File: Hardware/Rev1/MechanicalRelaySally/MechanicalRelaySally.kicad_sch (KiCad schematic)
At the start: 0 parts

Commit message: A
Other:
- added sheet Microcontroller (microcontroller.kicad_sch)
- sheet Power Routing ports: added CONTROL_BUS; removed none
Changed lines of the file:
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@@
 	(generator_version "9.0")
 	(paper "A4")
+	(bus
+		(pts
+			(xy 81.28 53.34) (xy 101.6 53.34)
+		)
+		(stroke
+			(width 0)
+			(type default)
+		)
+	)
 	(sheet
-		(at 132.08 25.4)
+		(at 53.34 50.8)
 		(size 27.94 22.86)
 		(exclude_from_sim no)
@@
 		)
 		(property "Sheetname" "Power Routing"
-			(at 132.08 24.6884 0)
+			(at 53.34 50.0884 0)
 			(effects
 				(font
@@
 		)
 		(property "Sheetfile" "power_routing.kicad_sch"
-			(at 132.08 48.8446 0)
+			(at 53.34 74.2446 0)
 			(effects
 				(font
@@
 				)
 				(justify left top)
+			)
+		)
+		(pin "CONTROL_BUS" input
+			(at 81.28 53.34 0)
+			(effects
+				(font
+					(size 1.27 1.27)
+				)
+				(justify right)
 			)
 		)
@@
 				)
 			)
+		)
+	)
+	(sheet
+		(at 101.6 50.8)
+		(size 27.94 22.86)
+		(exclude_from_sim no)
+		(in_bom yes)
+		(on_board yes)
+		(dnp no)
+		(fields_autoplaced yes)
+		(stroke
+			(width 0.1524)
+			(type solid)
+		)
+		(fill
+			(color 255 255 194 1.0000)
+		)
+		(property "Sheetname" "Microcontroller"
+			(at 101.6 50.0884 0)
+			(effects
+				(font
+					(size 1.27 1.27)
+				)
+				(justify left bottom)
+			)
+		)
+		(property "Sheetfile" "microcontroller.kicad_sch"
+			(at 101.6 74.2446 0)
+			(effects
+				(font
+					(size 1.27 1.27)
+				)
+				(justify left top)
+			)
+		)
+		(pin "CONTROL_BUS" input
+			(at 101.6 53.34 180)
+			(effects
+				(font
+					(size 1.27 1.27)
+				)
+				(justify left)
+			)
+		)
+		(instances
+			(project "MechanicalRelaySally"
+				(path "/fc3bfb83-1db4-4bd1-b480-85f699496fec"
+					(page "8")
+				)
+			)

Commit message: A
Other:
- sheet Microcontroller ports: added CAP_RLY{RELAY_EN COIL_CUR STATUS CUR_SENSE}, DSCH_RES_HIGH_RLY{RELAY_EN COIL_CUR STATUS CUR_SENSE}, DSCH_RES_LOW_RLY{RELAY_EN COIL_CUR STATUS CUR_SENSE}, MTR_RLY{RELAY_EN COIL_CUR STATUS CUR_SENSE}; removed CONTROL_BUS
- sheet Power Routing ports: added CAP_RLY{RELAY_EN COIL_CUR STATUS CUR_SENSE}, DSCH_RES_HIGH_RLY{RELAY_EN COIL_CUR STATUS CUR_SENSE}, DSCH_RES_LOW_RLY{RELAY_EN COIL_CUR STATUS CUR_SENSE}, MTR_RLY{RELAY_EN COIL_CUR STATUS CUR_SENSE}; removed CONTROL_BUS
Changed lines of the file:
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@@
 	(generator_version "9.0")
 	(paper "A4")
-	(bus
-		(pts
-			(xy 81.28 53.34) (xy 101.6 53.34)
-		)
-		(stroke
-			(width 0)
-			(type default)
-		)
-	)
 	(sheet
-		(at 53.34 50.8)
-		(size 27.94 22.86)
+		(at 17.78 50.8)
+		(size 63.5 22.86)
 		(exclude_from_sim no)
 		(in_bom yes)
@@
 		)
 		(property "Sheetname" "Power Routing"
-			(at 53.34 50.0884 0)
+			(at 17.78 50.0884 0)
 			(effects
 				(font
@@
 		)
 		(property "Sheetfile" "power_routing.kicad_sch"
-			(at 53.34 74.2446 0)
+			(at 17.78 74.2446 0)
 			(effects
 				(font
@@
 			)
 		)
-		(pin "CONTROL_BUS" input
+		(pin "MTR_RLY{RELAY_EN COIL_CUR STATUS CUR_SENSE}" output
 			(at 81.28 53.34 0)
+			(effects
+				(font
+					(size 1.27 1.27)
+				)
+				(justify right)
+			)
+		)
+		(pin "DSCH_RES_HIGH_RLY{RELAY_EN COIL_CUR STATUS CUR_SENSE}" output
+			(at 81.28 55.88 0)
+			(effects
+				(font
+					(size 1.27 1.27)
+				)
+				(justify right)
+			)
+		)
+		(pin "DSCH_RES_LOW_RLY{RELAY_EN COIL_CUR STATUS CUR_SENSE}" output
+			(at 81.28 58.42 0)
+			(effects
+				(font
+					(size 1.27 1.27)
+				)
+				(justify right)
+			)
+		)
+		(pin "CAP_RLY{RELAY_EN COIL_CUR STATUS CUR_SENSE}" output
+			(at 81.28 60.96 0)
 			(effects
 				(font
@@
 			)
 		)
-		(pin "CONTROL_BUS" input
+		(pin "CAP_RLY{RELAY_EN COIL_CUR STATUS CUR_SENSE}" input
+			(at 101.6 60.96 180)
+			(effects
+				(font
+					(size 1.27 1.27)
+				)
+				(justify left)
+			)
+		)
+		(pin "DSCH_RES_HIGH_RLY{RELAY_EN COIL_CUR STATUS CUR_SENSE}" input
+			(at 101.6 55.88 180)
+			(effects
+				(font
+					(size 1.27 1.27)
+				)
+				(justify left)
+			)
+		)
+		(pin "DSCH_RES_LOW_RLY{RELAY_EN COIL_CUR STATUS CUR_SENSE}" input
+			(at 101.6 58.42 180)
+			(effects
+				(font
+					(size 1.27 1.27)
+				)
+				(justify left)
+			)
+		)
+		(pin "MTR_RLY{RELAY_EN COIL_CUR STATUS CUR_SENSE}" input
 			(at 101.6 53.34 180)
 			(effects

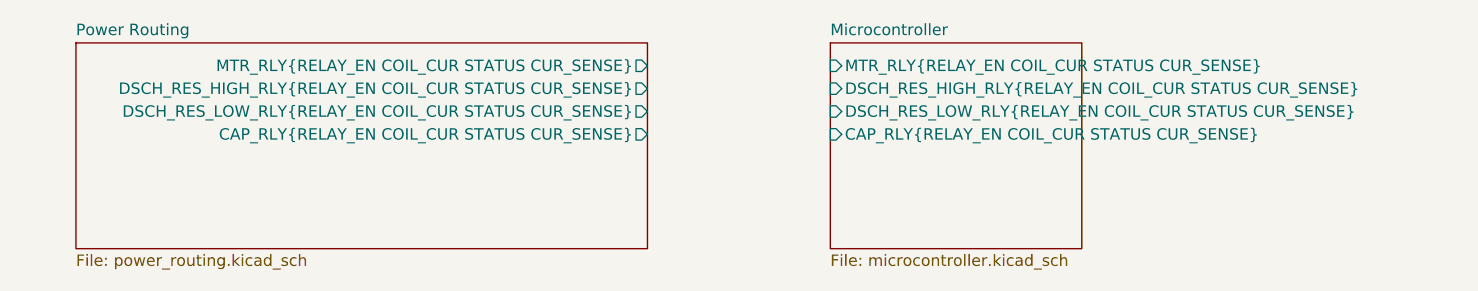
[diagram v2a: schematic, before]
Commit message: Added powerpole
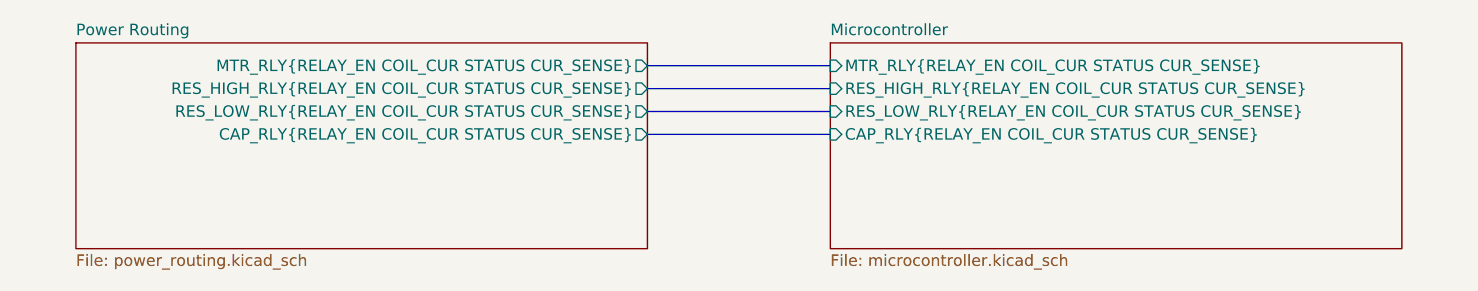
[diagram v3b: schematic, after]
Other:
- sheet Microcontroller ports: added RES_HIGH_RLY{RELAY_EN COIL_CUR STATUS CUR_SENSE}, RES_LOW_RLY{RELAY_EN COIL_CUR STATUS CUR_SENSE}; removed DSCH_RES_HIGH_RLY{RELAY_EN COIL_CUR STATUS CUR_SENSE}, DSCH_RES_LOW_RLY{RELAY_EN COIL_CUR STATUS CUR_SENSE}
- sheet Power Routing ports: added RES_HIGH_RLY{RELAY_EN COIL_CUR STATUS CUR_SENSE}, RES_LOW_RLY{RELAY_EN COIL_CUR STATUS CUR_SENSE}; removed DSCH_RES_HIGH_RLY{RELAY_EN COIL_CUR STATUS CUR_SENSE}, DSCH_RES_LOW_RLY{RELAY_EN COIL_CUR STATUS CUR_SENSE}
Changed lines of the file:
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@@
 	(generator_version "9.0")
 	(paper "A4")
+	(bus
+		(pts
+			(xy 81.28 58.42) (xy 101.6 58.42)
+		)
+		(stroke
+			(width 0)
+			(type default)
+		)
+	)
+	(bus
+		(pts
+			(xy 81.28 60.96) (xy 101.6 60.96)
+		)
+		(stroke
+			(width 0)
+			(type default)
+		)
+	)
+	(bus
+		(pts
+			(xy 81.28 53.34) (xy 101.6 53.34)
+		)
+		(stroke
+			(width 0)
+			(type default)
+		)
+	)
+	(bus
+		(pts
+			(xy 81.28 55.88) (xy 101.6 55.88)
+		)
+		(stroke
+			(width 0)
+			(type default)
+		)
+	)
 	(sheet
 		(at 17.78 50.8)
@@
 			)
 		)
-		(pin "DSCH_RES_HIGH_RLY{RELAY_EN COIL_CUR STATUS CUR_SENSE}" output
-			(at 81.28 55.88 0)
+		(pin "CAP_RLY{RELAY_EN COIL_CUR STATUS CUR_SENSE}" output
+			(at 81.28 60.96 0)
 			(effects
 				(font
@@
 			)
 		)
-		(pin "DSCH_RES_LOW_RLY{RELAY_EN COIL_CUR STATUS CUR_SENSE}" output
+		(pin "RES_LOW_RLY{RELAY_EN COIL_CUR STATUS CUR_SENSE}" output
 			(at 81.28 58.42 0)
 			(effects
@@
 			)
 		)
-		(pin "CAP_RLY{RELAY_EN COIL_CUR STATUS CUR_SENSE}" output
-			(at 81.28 60.96 0)
+		(pin "RES_HIGH_RLY{RELAY_EN COIL_CUR STATUS CUR_SENSE}" output
+			(at 81.28 55.88 0)
 			(effects
 				(font
@@
 	(sheet
 		(at 101.6 50.8)
-		(size 27.94 22.86)
+		(size 63.5 22.86)
 		(exclude_from_sim no)
 		(in_bom yes)
@@
 			)
 		)
-		(pin "DSCH_RES_HIGH_RLY{RELAY_EN COIL_CUR STATUS CUR_SENSE}" input
+		(pin "MTR_RLY{RELAY_EN COIL_CUR STATUS CUR_SENSE}" input
+			(at 101.6 53.34 180)
+			(effects
+				(font
+					(size 1.27 1.27)
+				)
+				(justify left)
+			)
+		)
+		(pin "RES_HIGH_RLY{RELAY_EN COIL_CUR STATUS CUR_SENSE}" input
 			(at 101.6 55.88 180)
 			(effects
@@
 			)
 		)
-		(pin "DSCH_RES_LOW_RLY{RELAY_EN COIL_CUR STATUS CUR_SENSE}" input
+		(pin "RES_LOW_RLY{RELAY_EN COIL_CUR STATUS CUR_SENSE}" input
 			(at 101.6 58.42 180)
 			(effects
 				(font
-					(size 1.27 1.27)
-				)
-				(justify left)
-			)
-		)
-		(pin "MTR_RLY{RELAY_EN COIL_CUR STATUS CUR_SENSE}" input
-			(at 101.6 53.34 180)
-			(effects
-				(font

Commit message: A
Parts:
- added H1, H2, H3, H4: MountingHole, MountingHole:MountingHole_3mm_Pad_Via, symbol Mechanical:MountingHole

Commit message: A
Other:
- sheet Microcontroller ports: added TEMP_BOARD_CENTER, TEMP_BOARD_VIN_DIODE; removed none
- sheet Power Routing ports: added TEMP_BOARD_CENTER, TEMP_BOARD_VIN_DIODE; removed none
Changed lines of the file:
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@@
+		)
+	)
+	(wire
+		(pts
+			(xy 81.28 63.5) (xy 101.6 63.5)
+		)
+		(stroke
+			(width 0)
+			(type default)
 		)
 	)
@@
 		(pts
 			(xy 81.28 55.88) (xy 101.6 55.88)
+		)
+		(stroke
+			(width 0)
+			(type default)
+		)
+	)
+	(wire
+		(pts
+			(xy 81.28 66.04) (xy 101.6 66.04)
 		)
 		(stroke
@@
 			)
 		)
+		(pin "TEMP_BOARD_CENTER" output
+			(at 81.28 63.5 0)
+			(effects
+				(font
+					(size 1.27 1.27)
+				)
+				(justify right)
+			)
+		)
+		(pin "TEMP_BOARD_VIN_DIODE" output
+			(at 81.28 66.04 0)
+			(effects
+				(font
+					(size 1.27 1.27)
+				)
+				(justify right)
+			)
+		)
 		(instances
 			(project "MechanicalRelaySally"
@@
 			(effects
 				(font
+					(size 1.27 1.27)
+				)
+				(justify left)
+			)
+		)
+		(pin "TEMP_BOARD_VIN_DIODE" output
+			(at 101.6 66.04 180)
+			(effects
+				(font
+					(size 1.27 1.27)
+				)
+				(justify left)
+			)
+		)
+		(pin "TEMP_BOARD_CENTER" output
+			(at 101.6 63.5 180)
+			(effects
+				(font

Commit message: A
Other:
- added sheet Measurement Buffers (measurment_buffers.kicad_sch)
- sheet Microcontroller ports: added FC_RLY{FC_EN FC_CUR}, VOLT_MEAS_BUF{FC_UP FC_OUT CAP RES_HIGH RES_LOW MTR_OUT}; removed none
- sheet Power Routing ports: added FC_RLY{FC_EN FC_CUR}, VOLT_MEAS{FC_UP FC_OUT CAP RES_HIGH RES_LOW MTR_OUT}; removed none
- moved on the sheet: H1, H2, H3, H4
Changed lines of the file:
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@@
 	(bus
 		(pts
-			(xy 81.28 58.42) (xy 101.6 58.42)
+			(xy 182.88 101.6) (xy 215.9 101.6)
+		)
+		(stroke
+			(width 0)
+			(type default)
+		)
+	)
+	(bus
+		(pts
+			(xy 81.28 83.82) (xy 215.9 83.82)
 		)
 		(stroke
@@
 	(wire
 		(pts
-			(xy 81.28 63.5) (xy 101.6 63.5)
+			(xy 81.28 88.9) (xy 215.9 88.9)
 		)
 		(stroke
@@
 	(bus
 		(pts
-			(xy 81.28 60.96) (xy 101.6 60.96)
+			(xy 81.28 86.36) (xy 215.9 86.36)
 		)
 		(stroke
@@
 	(bus
 		(pts
-			(xy 81.28 53.34) (xy 101.6 53.34)
+			(xy 81.28 78.74) (xy 215.9 78.74)
 		)
 		(stroke
@@
 	(bus
 		(pts
-			(xy 81.28 55.88) (xy 101.6 55.88)
+			(xy 81.28 104.14) (xy 114.3 104.14)
+		)
+		(stroke
+			(width 0)
+			(type default)
+		)
+	)
+	(bus
+		(pts
+			(xy 81.28 81.28) (xy 215.9 81.28)
 		)
 		(stroke
@@
 	(wire
 		(pts
-			(xy 81.28 66.04) (xy 101.6 66.04)
+			(xy 81.28 91.44) (xy 215.9 91.44)
+		)
+		(stroke
+			(width 0)
+			(type default)
+		)
+	)
+	(bus
+		(pts
+			(xy 81.28 93.98) (xy 215.9 93.98)
 		)
 		(stroke
@@
 	(symbol
 		(lib_id "Mechanical:MountingHole")
-		(at 44.45 110.49 0)
+		(at 137.16 144.78 0)
 		(unit 1)
 		(exclude_from_sim no)
@@
 		(fields_autoplaced yes)
 		(property "Reference" "H3"
-			(at 46.99 109.2199 0)
+			(at 139.7 143.5099 0)
 			(effects
 				(font
@@
 		)
 		(property "Value" "MountingHole"
-			(at 46.99 111.7599 0)
+			(at 139.7 146.0499 0)
 			(effects
 				(font
@@
 		)
 		(property "Footprint" "MountingHole:MountingHole_3mm_Pad_Via"
-			(at 44.45 110.49 0)
+			(at 137.16 144.78 0)
 			(effects
 				(font
@@
 		)
 		(property "Datasheet" "~"
-			(at 44.45 110.49 0)
+			(at 137.16 144.78 0)
 			(effects
 				(font
@@
 		)
 		(property "Description" "Mounting Hole without connection"
-			(at 44.45 110.49 0)
+			(at 137.16 144.78 0)
 			(effects
 				(font
@@
 	(symbol
 		(lib_id "Mechanical:MountingHole")
-		(at 44.45 97.79 0)
+		(at 137.16 132.08 0)
 		(unit 1)
 		(exclude_from_sim no)
@@
 		(fields_autoplaced yes)
 		(property "Reference" "H1"
-			(at 46.99 96.5199 0)
+			(at 139.7 130.8099 0)
 			(effects
 				(font
@@
 		)
 		(property "Value" "MountingHole"
-			(at 46.99 99.0599 0)
+			(at 139.7 133.3499 0)
 			(effects
 				(font
@@
 		)
 		(property "Footprint" "MountingHole:MountingHole_3mm_Pad_Via"
-			(at 44.45 97.79 0)
+			(at 137.16 132.08 0)
 			(effects
 				(font
@@
 		)
 		(property "Datasheet" "~"
-			(at 44.45 97.79 0)
+			(at 137.16 132.08 0)
 			(effects
 				(font
@@
 		)
 		(property "Description" "Mounting Hole without connection"
-			(at 44.45 97.79 0)
+			(at 137.16 132.08 0)
 			(effects
 				(font
@@
 	(symbol
 		(lib_id "Mechanical:MountingHole")
-		(at 44.45 116.84 0)
+		(at 137.16 151.13 0)
 		(unit 1)
 		(exclude_from_sim no)
@@
 		(fields_autoplaced yes)
 		(property "Reference" "H4"
-			(at 46.99 115.5699 0)
+			(at 139.7 149.8599 0)
 			(effects
 				(font
@@
 		)
 		(property "Value" "MountingHole"
-			(at 46.99 118.1099 0)
+			(at 139.7 152.3999 0)
 			(effects
 				(font
@@
 		)
 		(property "Footprint" "MountingHole:MountingHole_3mm_Pad_Via"
-			(at 44.45 116.84 0)
+			(at 137.16 151.13 0)
 			(effects
 				(font
@@
 		)
 		(property "Datasheet" "~"
-			(at 44.45 116.84 0)
+			(at 137.16 151.13 0)
 			(effects
 				(font
@@
 		)
 		(property "Description" "Mounting Hole without connection"
-			(at 44.45 116.84 0)
+			(at 137.16 151.13 0)
 			(effects
 				(font
@@
 	(symbol
 		(lib_id "Mechanical:MountingHole")
-		(at 44.45 104.14 0)
+		(at 137.16 138.43 0)
 		(unit 1)
 		(exclude_from_sim no)
@@
 		(fields_autoplaced yes)
 		(property "Reference" "H2"
-			(at 46.99 102.8699 0)
+			(at 139.7 137.1599 0)
 			(effects
 				(font
@@
 		)
 		(property "Value" "MountingHole"
-			(at 46.99 105.4099 0)
+			(at 139.7 139.6999 0)
 			(effects
 				(font
@@
 		)
 		(property "Footprint" "MountingHole:MountingHole_3mm_Pad_Via"
-			(at 44.45 104.14 0)
+			(at 137.16 138.43 0)
 			(effects
 				(font
@@
 		)
 		(property "Datasheet" "~"
-			(at 44.45 104.14 0)
+			(at 137.16 138.43 0)
 			(effects
 				(font
@@
 		)
 		(property "Description" "Mounting Hole without connection"
-			(at 44.45 104.14 0)
+			(at 137.16 138.43 0)
 			(effects
 				(font
@@
 	)
 	(sheet
-		(at 17.78 50.8)
-		(size 63.5 22.86)
+		(at 17.78 76.2)
+		(size 63.5 33.02)
 		(exclude_from_sim no)
 		(in_bom yes)
@@
 		)
 		(property "Sheetname" "Power Routing"
-			(at 17.78 50.0884 0)
+			(at 17.78 75.4884 0)
 			(effects
 				(font
@@
 		)
 		(property "Sheetfile" "power_routing.kicad_sch"
-			(at 17.78 74.2446 0)
+			(at 17.78 109.8046 0)
 			(effects
 				(font
@@
 		)
 		(pin "MTR_RLY{RELAY_EN COIL_CUR STATUS CUR_SENSE}" output
-			(at 81.28 53.34 0)
+			(at 81.28 78.74 0)
 			(effects
 				(font
@@
 		)
 		(pin "CAP_RLY{RELAY_EN COIL_CUR STATUS CUR_SENSE}" output
-			(at 81.28 60.96 0)
+			(at 81.28 86.36 0)
 			(effects
 				(font
@@
 		)
 		(pin "RES_LOW_RLY{RELAY_EN COIL_CUR STATUS CUR_SENSE}" output
-			(at 81.28 58.42 0)
+			(at 81.28 83.82 0)
 			(effects
 				(font
@@
 		)
 		(pin "RES_HIGH_RLY{RELAY_EN COIL_CUR STATUS CUR_SENSE}" output
-			(at 81.28 55.88 0)
+			(at 81.28 81.28 0)
 			(effects
 				(font
@@
 		)
 		(pin "TEMP_BOARD_CENTER" output
-			(at 81.28 63.5 0)
+			(at 81.28 88.9 0)
 			(effects
 				(font
@@
 		)
 		(pin "TEMP_BOARD_VIN_DIODE" output
-			(at 81.28 66.04 0)
+			(at 81.28 91.44 0)
+			(effects
+				(font
+					(size 1.27 1.27)
+				)
+				(justify right)
+			)
+		)
+		(pin "FC_RLY{FC_EN FC_CUR}" output
+			(at 81.28 93.98 0)
+			(effects
+				(font
+					(size 1.27 1.27)
+				)
+				(justify right)
+			)
+		)
+		(pin "VOLT_MEAS{FC_UP FC_OUT CAP RES_HIGH RES_LOW MTR_OUT}" output
+			(at 81.28 104.14 0)
 			(effects
 				(font
@@
 	)
 	(sheet
-		(at 101.6 50.8)
-		(size 63.5 22.86)
+		(at 114.3 99.06)
+		(size 68.58 17.78)
 		(exclude_from_sim no)
 		(in_bom yes)
@@
 			(color 255 255 194 1.0000)
 		)
+		(property "Sheetname" "Measurement Buffers"
+			(at 114.3 98.3484 0)
+			(effects
+				(font
+					(size 1.27 1.27)
+				)
+				(justify left bottom)
+			)
+		)
+		(property "Sheetfile" "measurment_buffers.kicad_sch"
+			(at 114.3 117.4246 0)
+			(effects
+				(font
+					(size 1.27 1.27)
+				)
+				(justify left top)
+			)
+		)
+		(pin "VOLT_MEAS{FC_UP FC_OUT CAP RES_HIGH RES_LOW MTR_OUT}" output
+			(at 114.3 104.14 180)
+			(effects
+				(font
+					(size 1.27 1.27)
+				)
+				(justify left)
+			)
+		)
+		(pin "VOLT_MEAS_BUF{FC_UP FC_OUT CAP RES_HIGH RES_LOW MTR_OUT}" output
+			(at 182.88 101.6 0)
+			(effects
+				(font
+					(size 1.27 1.27)
+				)
+				(justify right)
+			)
+		)
+		(instances
+			(project "MechanicalRelaySally"
+				(path "/fc3bfb83-1db4-4bd1-b480-85f699496fec"
+					(page "8")
+				)
+			)
+		)
+	)
+	(sheet
+		(at 215.9 76.2)
+		(size 66.675 33.02)
+		(exclude_from_sim no)
+		(in_bom yes)
+		(on_board yes)
+		(dnp no)
+		(fields_autoplaced yes)
+		(stroke
+			(width 0.1524)
+			(type solid)
+		)
+		(fill
+			(color 255 255 194 1.0000)
+		)
 		(property "Sheetname" "Microcontroller"
-			(at 101.6 50.0884 0)
+			(at 215.9 75.4884 0)
 			(effects
 				(font
@@
 		)
 		(property "Sheetfile" "microcontroller.kicad_sch"
-			(at 101.6 74.2446 0)
+			(at 215.9 109.8046 0)
 			(effects
 				(font
@@
 		)
 		(pin "CAP_RLY{RELAY_EN COIL_CUR STATUS CUR_SENSE}" input
-			(at 101.6 60.96 180)
+			(at 215.9 86.36 180)
 			(effects
 				(font
@@
 		)
 		(pin "MTR_RLY{RELAY_EN COIL_CUR STATUS CUR_SENSE}" input
-			(at 101.6 53.34 180)
+			(at 215.9 78.74 180)
 			(effects
 				(font
@@
 		)
 		(pin "RES_HIGH_RLY{RELAY_EN COIL_CUR STATUS CUR_SENSE}" input
-			(at 101.6 55.88 180)
+			(at 215.9 81.28 180)
 			(effects
 				(font
@@
 		)
 		(pin "RES_LOW_RLY{RELAY_EN COIL_CUR STATUS CUR_SENSE}" input
-			(at 101.6 58.42 180)
+			(at 215.9 83.82 180)
 			(effects
 				(font
@@
 		)
 		(pin "TEMP_BOARD_VIN_DIODE" output
-			(at 101.6 66.04 180)
+			(at 215.9 91.44 180)
 			(effects
 				(font
@@
 		)
 		(pin "TEMP_BOARD_CENTER" output
-			(at 101.6 63.5 180)
-			(effects
-				(font
+			(at 215.9 88.9 180)
+			(effects
+				(font
+					(size 1.27 1.27)
+				)
+				(justify left)
+			)
+		)
+		(pin "FC_RLY{FC_EN FC_CUR}" output
+			(at 215.9 93.98 180)
+			(effects
+				(font
+					(size 1.27 1.27)
+				)
+				(justify left)
+			)
+		)
+		(pin "VOLT_MEAS_BUF{FC_UP FC_OUT CAP RES_HIGH RES_LOW MTR_OUT}" output
+			(at 215.9 101.6 180)
+			(effects
+				(font

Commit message: A
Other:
- added sheet Power Regulation (power_regulation.kicad_sch)
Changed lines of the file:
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@@
+	)
+	(sheet
+		(at 17.78 34.29)
+		(size 63.5 29.21)
+		(exclude_from_sim no)
+		(in_bom yes)
+		(on_board yes)
+		(dnp no)
+		(fields_autoplaced yes)
+		(stroke
+			(width 0.1524)
+			(type solid)
+		)
+		(fill
+			(color 255 255 194 1.0000)
+		)
+		(property "Sheetname" "Power Regulation"
+			(at 17.78 33.5784 0)
+			(effects
+				(font
+					(size 1.27 1.27)
+				)
+				(justify left bottom)
+			)
+		)
+		(property "Sheetfile" "power_regulation.kicad_sch"
+			(at 17.78 64.0846 0)
+			(effects
+				(font
+					(size 1.27 1.27)
+				)
+				(justify left top)
+			)
+		)
+		(instances
+			(project "MechanicalRelaySally"
+				(path "/fc3bfb83-1db4-4bd1-b480-85f699496fec"
+					(page "9")
+				)
+			)
+		)
 	)
 	(sheet
